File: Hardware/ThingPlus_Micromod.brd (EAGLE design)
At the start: 91.4 x 22.9 mm, 152 parts, among them J4 QWIIC_RIGHT_ANGLE, J5 MICRO-SD-SDIOPUSH-PUSH, J6 JTAG, J7 MICROMOD-2222-C, U2 MCP73831, U3 MAX17048, U4 3.3V, U6 AP7361C-33

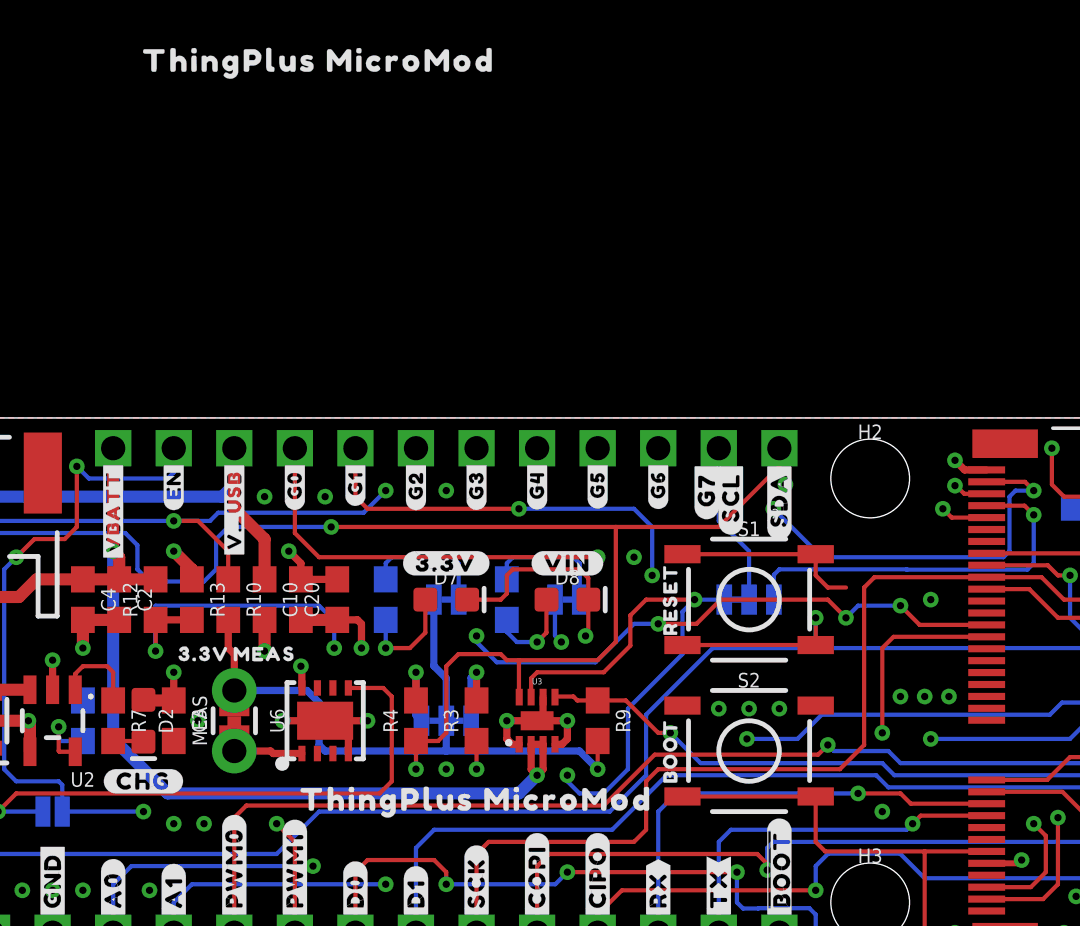
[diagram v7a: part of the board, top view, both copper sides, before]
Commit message: Updated labeling placement.
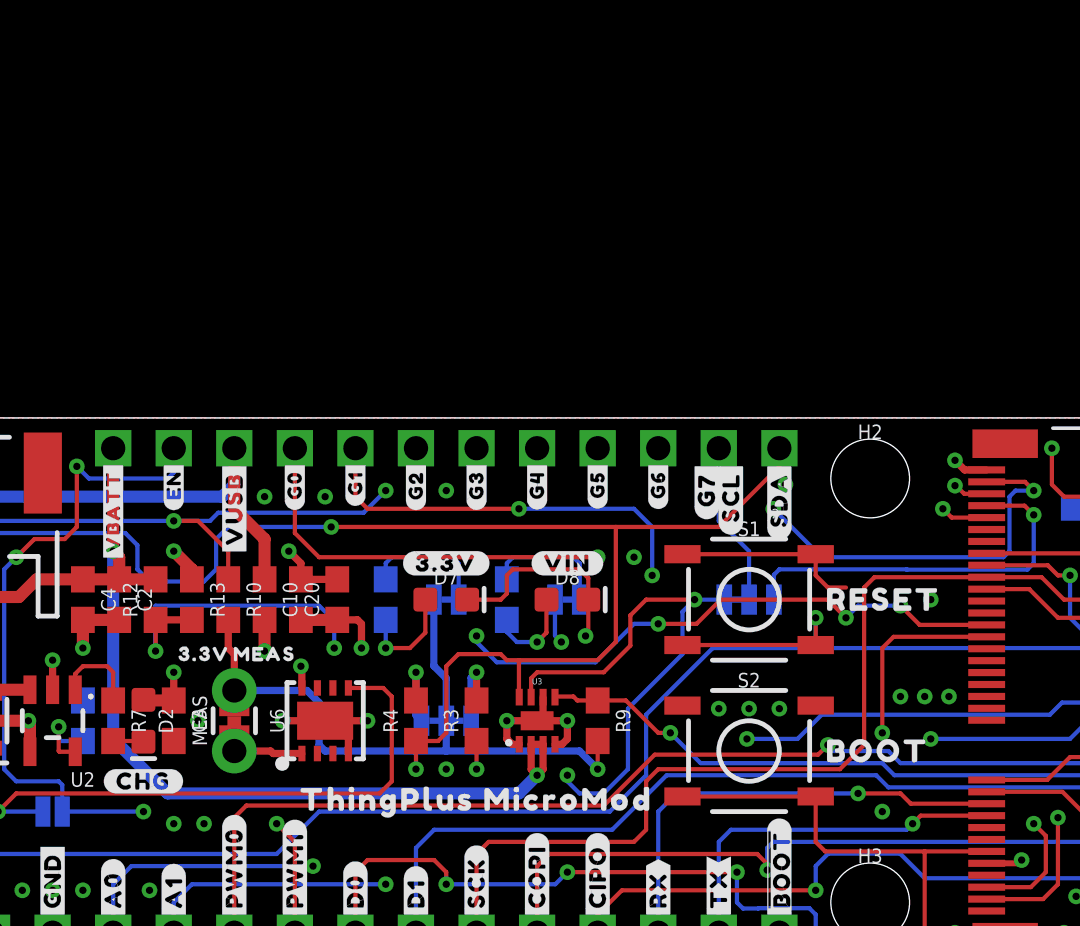
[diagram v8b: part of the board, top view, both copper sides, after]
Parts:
- removed U$69: (no value), output:THINGPLUS_MICROMOD25
- U$23: device output:BOOT14 -> output:BOOT16
- U$24: device output:RESET15 -> output:RESET17
- U$27, U$58: device output:#V_USB#12 -> output:#VUSB#13
- moved U$23 5.84 mm to (53.3, 8.89), turned to 0 degrees
- moved U$24 5.84 mm to (53.3, 15.2), turned to 0 degrees
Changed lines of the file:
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@@
 <setting verticaltext="up"/>
 </settings>
-<grid distance="0.05" unitdist="inch" unit="mil" style="lines" multiple="1" display="yes" altdistance="0.005" altunitdist="inch" altunit="mil"/>
+<grid distance="10" unitdist="mil" unit="mil" style="lines" multiple="1" display="yes" altdistance="0.005" altunitdist="inch" altunit="mil"/>
 <layers>
-<layer number="1" name="Top" color="4" fill="1" visible="no" active="yes"/>
+<layer number="1" name="Top" color="4" fill="1" visible="yes" active="yes"/>
 <layer number="2" name="Route2" color="16" fill="1" visible="no" active="yes"/>
 <layer number="15" name="Route15" color="23" fill="1" visible="no" active="yes"/>
-<layer number="16" name="Bottom" color="1" fill="1" visible="no" active="yes"/>
+<layer number="16" name="Bottom" color="1" fill="1" visible="yes" active="yes"/>
 <layer number="17" name="Pads" color="2" fill="1" visible="yes" active="yes"/>
 <layer number="18" name="Vias" color="2" fill="1" visible="yes" active="yes"/>
@@
 <element name="U$21" library="output" package="#TX#9" value="" x="49.53" y="1.778" smashed="yes" rot="R90"/>
 <element name="U$22" library="output" package="##BOOT##10" value="" x="52.07" y="1.778" smashed="yes" rot="R90"/>
-<element name="U$23" library="output" package="BOOT14" value="" x="47.498" y="8.89" smashed="yes" rot="R90"/>
-<element name="U$24" library="output" package="RESET15" value="" x="47.498" y="15.24" smashed="yes" rot="R90"/>
 <element name="U$25" library="output" package="#VBATT#13" value="" x="24.13" y="21.082" smashed="yes" rot="R90"/>
 <element name="U$26" library="output" package="#EN#13" value="" x="26.67" y="21.082" smashed="yes" rot="R90"/>
-<element name="U$27" library="output" package="#V_USB#12" value="" x="29.21" y="21.082" smashed="yes" rot="R90"/>
 <element name="U$28" library="output" package="#G0#12" value="" x="31.75" y="21.082" smashed="yes" rot="R90"/>
 <element name="U$29" library="output" package="#G1#12" value="" x="34.29" y="21.082" smashed="yes" rot="R90"/>
@@
 <element name="U$56" library="output" package="#VBATT#13" value="" x="24.13" y="21.082" smashed="yes" rot="MR90"/>
 <element name="U$57" library="output" package="#EN#13" value="" x="26.67" y="21.082" smashed="yes" rot="MR90"/>
-<element name="U$58" library="output" package="#V_USB#12" value="" x="29.21" y="21.082" smashed="yes" rot="MR90"/>
 <element name="U$59" library="output" package="#G0#12" value="" x="31.75" y="21.082" smashed="yes" rot="MR90"/>
 <element name="U$60" library="output" package="#G1#12" value="" x="34.29" y="21.082" smashed="yes" rot="MR90"/>
@@
 <element name="U$67" library="output" package="#G7#13" value="" x="49.022" y="21.082" smashed="yes" rot="MR90"/>
 <element name="U$68" library="output" package="#SCL#12" value="" x="50.038" y="21.082" smashed="yes" rot="MR90"/>
-<element name="U$69" library="output" package="THINGPLUS_MICROMOD25" value="" x="32.766" y="37.846" smashed="yes"/>
 <element name="U$70" library="output" package="#3#3V_EN#22" value="" x="21.59" y="8.001" smashed="yes" rot="MR0"/>
 <element name="U$71" library="output" package="#3#3V#21" value="" x="38.1" y="16.764" smashed="yes" rot="MR0"/>
@@
 <element name="U$80" library="output" package="THINGPLUS_MICROMOD25" value="" x="50.8" y="11.43" smashed="yes" rot="MR0"/>
 <element name="U$2" library="SparkX" package="SPARKX-MEDIUM" value="SPARKX-LOGO4" x="50.8" y="8.89" smashed="yes" rot="MR0"/>
+<element name="U$23" library="output" package="BOOT16" value="" x="53.34" y="8.89" smashed="yes"/>
+<element name="U$24" library="output" package="RESET17" value="" x="53.34" y="15.24" smashed="yes"/>
+<element name="U$27" library="output" package="#VUSB#13" value="" x="29.21" y="21.082" smashed="yes" rot="R90"/>
+<element name="U$58" library="output" package="#VUSB#13" value="" x="29.21" y="21.082" smashed="yes" rot="MR90"/>
 </elements>
 <signals>
